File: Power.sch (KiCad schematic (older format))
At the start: 18 parts, among them P1 24 Pin MiniFit JR, SW1 Power Switch

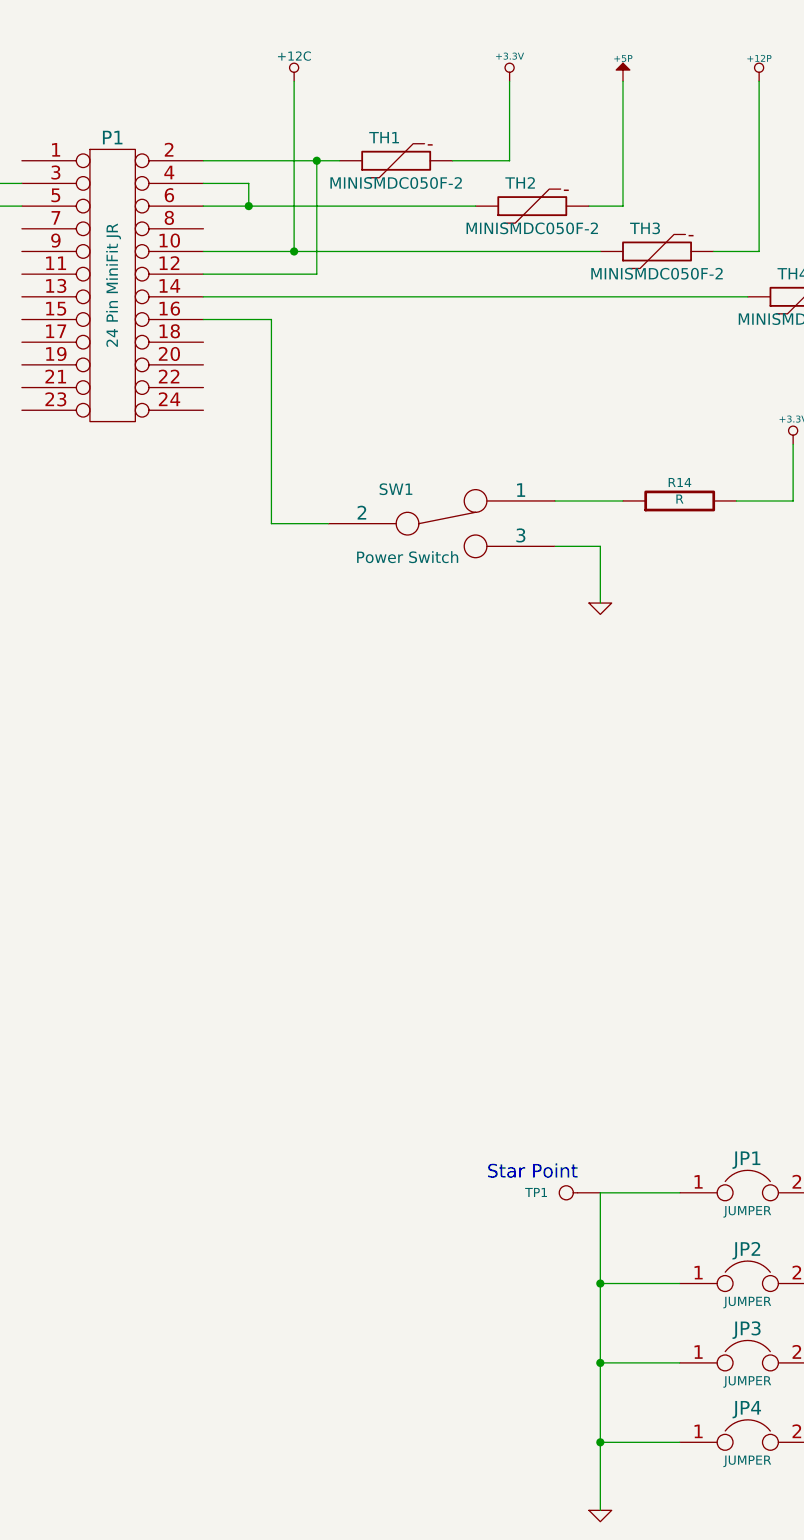
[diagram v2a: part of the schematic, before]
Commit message: Layout Work Session 16
Added ground connect to heatsink, fixed relay trace width, fixed silk
screen issues.
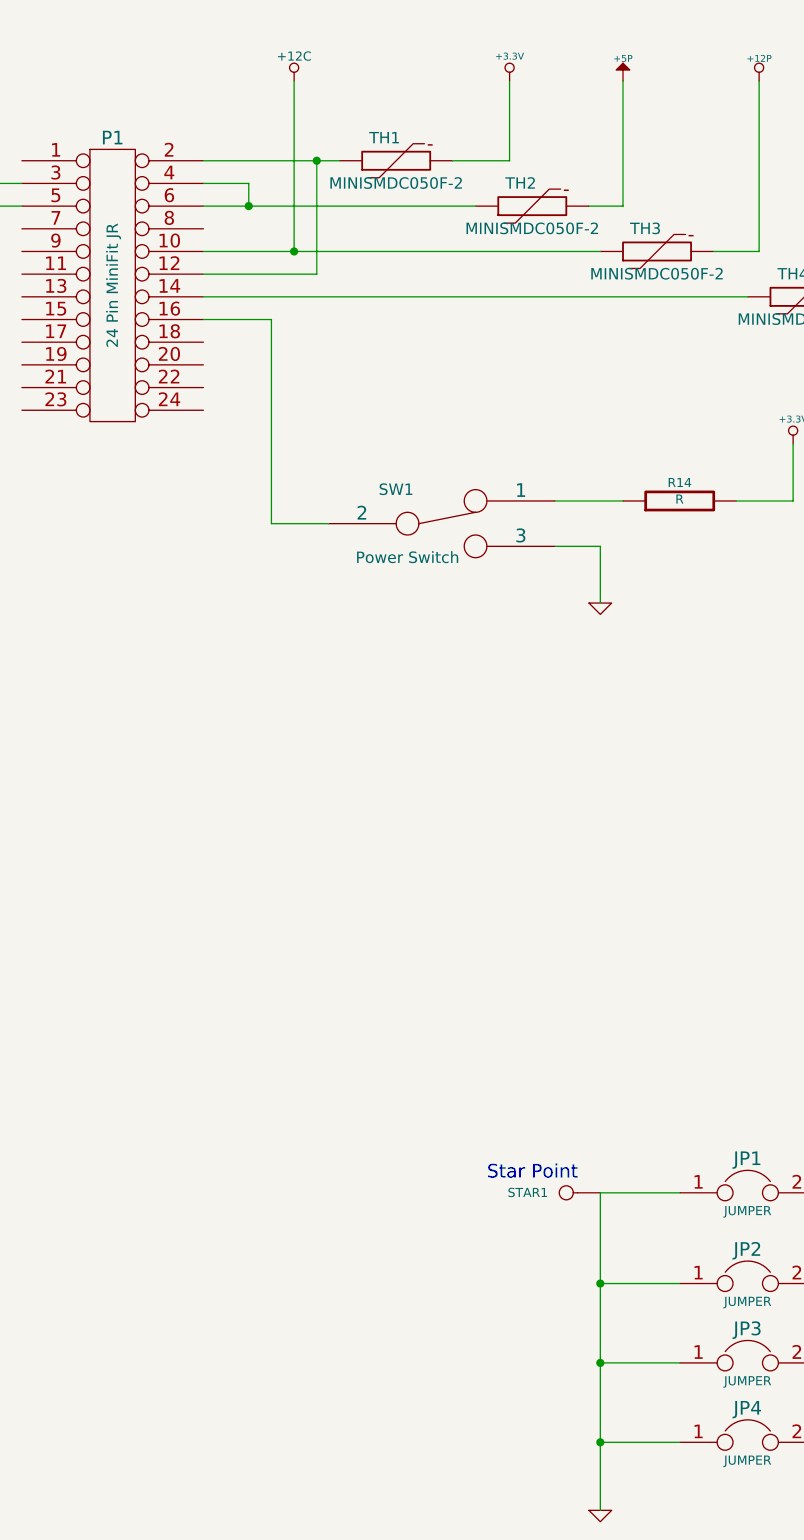
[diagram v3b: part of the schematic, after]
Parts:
- renumbered TP1 to STAR1
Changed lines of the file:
@@
-EESchema Schematic File Version 2  date 11/24/2013 8:21:44 PM
+EESchema Schematic File Version 2  date 12/1/2013 9:10:28 PM
 LIBS:power
 LIBS:device
@@
 Sheet 9 9
 Title ""
-Date "24 nov 2013"
+Date "2 dec 2013"
 Rev ""
 Comp ""
@@
 $EndComp
 $Comp
-L GND #PWR045
+L GND #PWR53
 U 1 1 523DFA76
 P 1400 1850
-F 0 "#PWR045" H 1400 1850 30  0001 C CNN
+F 0 "#PWR53" H 1400 1850 30  0001 C CNN
 F 1 "GND" H 1400 1780 30  0001 C CNN
 F 2 "" H 1400 1850 60  0000 C CNN
@@
 	1400 1600 1400 1850
 Wire Wire Line
-	3650 1500 3050 1500
+	3050 1500 3650 1500
 Wire Wire Line
 	4150 1500 4400 1500
@@
 	5500 1900 5500 1150
 $Comp
-L +12P #PWR046
+L +12P #PWR59
 U 1 1 523DFB91
 P 5500 1150
-F 0 "#PWR046" H 5500 1120 30  0001 C CNN
+F 0 "#PWR59" H 5500 1120 30  0001 C CNN
 F 1 "+12P" H 5500 1250 30  0000 C CNN
 F 2 "" H 5500 1150 60  0000 C CNN
@@
 $EndComp
 $Comp
-L -12P #PWR047
+L -12P #PWR61
 U 1 1 523E04D8
 P 6100 1150
-F 0 "#PWR047" H 6100 1280 20  0001 C CNN
+F 0 "#PWR61" H 6100 1280 20  0001 C CNN
 F 1 "-12P" H 6100 1250 30  0000 C CNN
 F 2 "" H 6100 1150 60  0000 C CNN
@@
 	4800 3200 4800 3450
 $Comp
-L GND #PWR048
+L GND #PWR56
 U 1 1 523E08C4
 P 4800 3450
-F 0 "#PWR048" H 4800 3450 30  0001 C CNN
+F 0 "#PWR56" H 4800 3450 30  0001 C CNN
 F 1 "GND" H 4800 3380 30  0001 C CNN
 F 2 "" H 4800 3450 60  0000 C CNN
@@
 	5650 3000 5650 2750
 $Comp
-L +3.3V #PWR049
+L +3.3V #PWR60
 U 1 1 523E0910
 P 5650 2750
-F 0 "#PWR049" H 5650 2710 30  0001 C CNN
+F 0 "#PWR60" H 5650 2710 30  0001 C CNN
 F 1 "+3.3V" H 5650 2860 30  0000 C CNN
 F 2 "" H 5650 2750 60  0000 C CNN
@@
 $EndComp
 $Comp
-L +12P #PWR050
+L +12P #PWR67
 U 1 1 523E0C76
 P 8000 2250
-F 0 "#PWR050" H 8000 2220 30  0001 C CNN
+F 0 "#PWR67" H 8000 2220 30  0001 C CNN
 F 1 "+12P" H 8000 2350 30  0000 C CNN
 F 2 "" H 8000 2250 60  0000 C CNN
@@
 $EndComp
 $Comp
-L -12P #PWR051
+L -12P #PWR68
 U 1 1 523E0C7C
 P 8000 3800
-F 0 "#PWR051" H 8000 3930 20  0001 C CNN
+F 0 "#PWR68" H 8000 3930 20  0001 C CNN
 F 1 "-12P" H 8000 3900 30  0000 C CNN
 F 2 "" H 8000 3800 60  0000 C CNN
@@
 $EndComp
 $Comp
-L GND #PWR052
+L GND #PWR69
 U 1 1 523E0C82
 P 9000 3200
-F 0 "#PWR052" H 9000 3200 30  0001 C CNN
+F 0 "#PWR69" H 9000 3200 30  0001 C CNN
 F 1 "GND" H 9000 3130 30  0001 C CNN
 F 2 "" H 9000 3200 60  0000 C CNN
@@
 Connection ~ 9450 3050
 $Comp
-L -12V #PWR053
+L -12V #PWR73
 U 1 1 523E0DD3
 P 10350 3800
-F 0 "#PWR053" H 10350 3930 20  0001 C CNN
+F 0 "#PWR73" H 10350 3930 20  0001 C CNN
 F 1 "-12V" H 10350 3900 30  0000 C CNN
 F 2 "" H 10350 3800 60  0000 C CNN
@@
 Connection ~ 9450 2450
 $Comp
-L +12V #PWR054
+L +12V #PWR72
 U 1 1 523E0E37
 P 10350 2200
-F 0 "#PWR054" H 10350 2150 20  0001 C CNN
+F 0 "#PWR72" H 10350 2150 20  0001 C CNN
 F 1 "+12V" H 10350 2300 30  0000 C CNN
 F 2 "" H 10350 2200 60  0000 C CNN
@@
 Connection ~ 3450 1900
 $Comp
-L +12C #PWR055
+L +12C #PWR54
 U 1 1 52438F0D
 P 3450 1150
-F 0 "#PWR055" H 3450 1120 30  0001 C CNN
+F 0 "#PWR54" H 3450 1120 30  0001 C CNN
 F 1 "+12C" H 3450 1260 40  0000 C CNN
 F 2 "~" H 3450 1150 60  0000 C CNN
@@
 $EndComp
 $Comp
-L GND #PWR056
+L GND #PWR70
 U 1 1 524502FC
 P 9400 1650
-F 0 "#PWR056" H 9400 1650 30  0001 C CNN
+F 0 "#PWR70" H 9400 1650 30  0001 C CNN
 F 1 "GND" H 9400 1580 30  0001 C CNN
 F 2 "" H 9400 1650 60  0000 C CNN
@@
 Connection ~ 9400 900
 $Comp
-L +5P #PWR56
+L +5P #PWR58
 U 1 1 52450355
 P 4900 1150
-F 0 "#PWR56" H 4900 1280 20  0001 C CNN
+F 0 "#PWR58" H 4900 1280 20  0001 C CNN
 F 1 "+5P" H 4900 1250 30  0000 C CNN
 F 2 "~" H 4900 1150 60  0000 C CNN
@@
 $EndComp
 $Comp
-L +5P #PWR64
+L +5P #PWR66
 U 1 1 52450371
 P 7950 700
-F 0 "#PWR64" H 7950 830 20  0001 C CNN
+F 0 "#PWR66" H 7950 830 20  0001 C CNN
 F 1 "+5P" H 7950 800 30  0000 C CNN
 F 2 "~" H 7950 700 60  0000 C CNN
@@
 $EndComp
 $Comp
-L +5V #PWR057
+L +5V #PWR71
 U 1 1 524503B6
 P 10300 650
-F 0 "#PWR057" H 10300 740 20  0001 C CNN
+F 0 "#PWR71" H 10300 740 20  0001 C CNN
 F 1 "+5V" H 10300 740 30  0000 C CNN
 F 2 "~" H 10300 650 60  0000 C CNN
@@
 $EndComp
 $Comp
-L +3.3V #PWR058
+L +3.3V #PWR55
 U 1 1 526E168C
 P 4400 1150
-F 0 "#PWR058" H 4400 1110 30  0001 C CNN
+F 0 "#PWR55" H 4400 1110 30  0001 C CNN
 F 1 "+3.3V" H 4400 1260 30  0000 C CNN
 F 2 "" H 4400 1150 60  0000 C CNN
@@
 Connection ~ 3550 1500
 $Comp
-L CONN_1 TP1
+L CONN_1 STAR1
 U 1 1 527EFE16
 P 4650 6050
-F 0 "TP1" H 4730 6050 40  0000 L CNN
+F 0 "STAR1" H 4730 6050 40  0000 L CNN
 F 1 "CONN_1" H 4650 6105 30  0001 C CNN
 F 2 "" H 4650 6050 60  0000 C CNN
@@
 $EndComp
 $Comp
-L GND #PWR059
+L GND #PWR57
 U 1 1 52804AA7
 P 4800 7450
-F 0 "#PWR059" H 4800 7450 30  0001 C CNN
+F 0 "#PWR57" H 4800 7450 30  0001 C CNN
 F 1 "GND" H 4800 7380 30  0001 C CNN
 F 2 "" H 4800 7450 60  0000 C CNN
@@
 $EndComp
 Wire Wire Line
-	4800 7450 4800 6050
+	4800 6050 4800 7450
 Wire Wire Line
 	4800 6050 5150 6050
@@
 	5750 6050 6200 6050
 $Comp
-L GND_RELAY #PWR060
+L GND_RELAY #PWR65
 U 1 1 52804C2C
 P 6200 7400
-F 0 "#PWR060" H 6200 7400 30  0001 C CNN
+F 0 "#PWR65" H 6200 7400 30  0001 C CNN
 F 1 "GND_RELAY" H 6200 7330 30  0000 C CNN
 F 2 "~" H 6200 7400 60  0000 C CNN
@@
 $EndComp
 $Comp
-L GND_LED #PWR061
+L GND_LED #PWR64
 U 1 1 52804C3B
 P 6200 6950
-F 0 "#PWR061" H 6200 6950 30  0001 C CNN
+F 0 "#PWR64" H 6200 6950 30  0001 C CNN
 F 1 "GND_LED" H 6200 6880 30  0000 C CNN
 F 2 "~" H 6200 6950 60  0000 C CNN
@@
 $EndComp
 $Comp
-L GND_PWR #PWR062
+L GND_PWR #PWR63
 U 1 1 52804C4A
 P 6200 6550
-F 0 "#PWR062" H 6200 6550 30  0001 C CNN
+F 0 "#PWR63" H 6200 6550 30  0001 C CNN
 F 1 "GND_PWR" H 6200 6480 30  0000 C CNN
 F 2 "~" H 6200 6550 60  0000 C CNN
@@
 $EndComp
 $Comp
-L AGND #PWR063
+L AGND #PWR62
 U 1 1 52804C59
 P 6200 6200
-F 0 "#PWR063" H 6200 6200 40  0001 C CNN
+F 0 "#PWR62" H 6200 6200 40  0001 C CNN
 F 1 "AGND" H 6200 6130 50  0000 C CNN
 F 2 "~" H 6200 6200 60  0000 C CNN

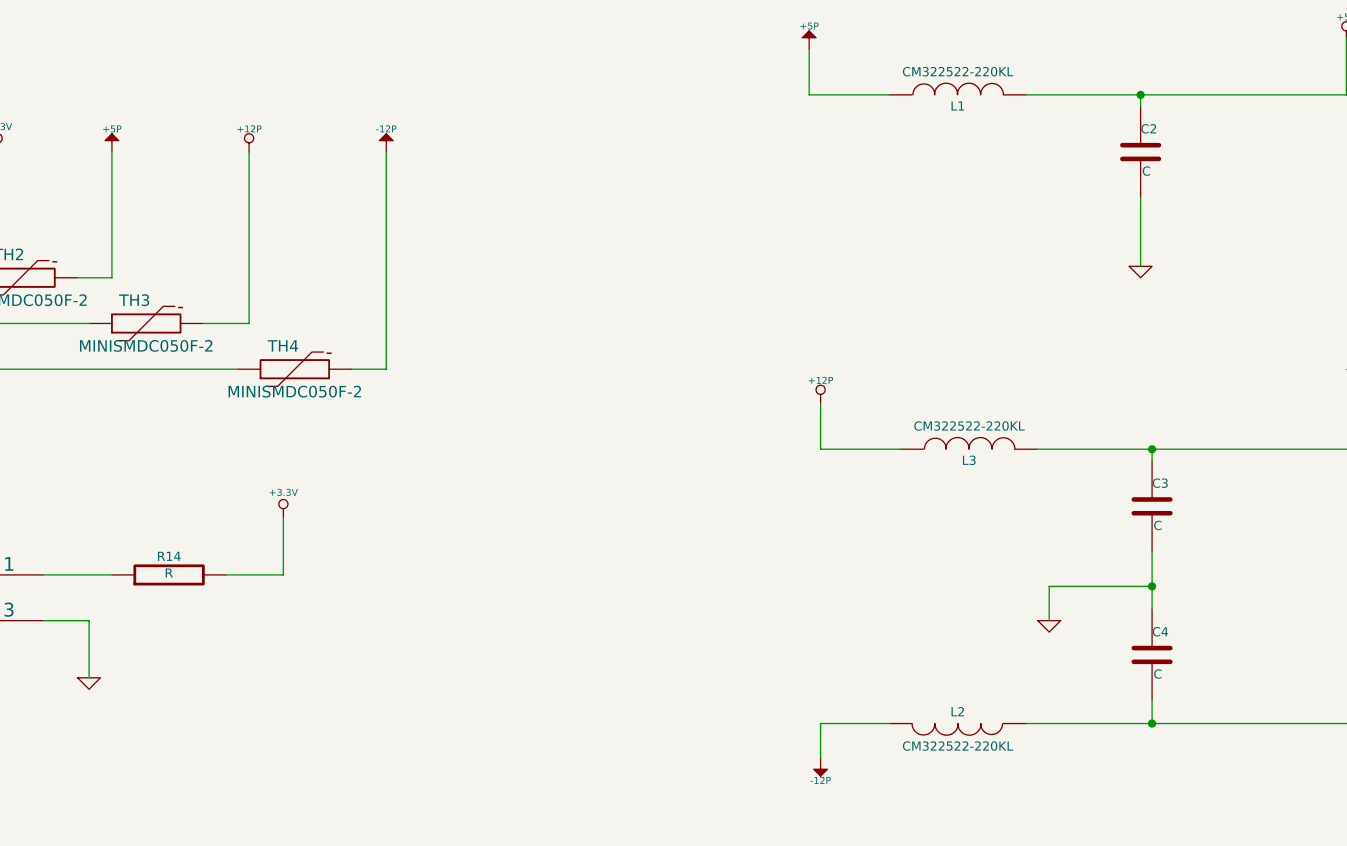
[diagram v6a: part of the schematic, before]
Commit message: Added Passive Values and SPICE models
As part of week 1 of Session 1B, we added a SPICE model of the In amp
and went through and assigned values to all of the passive components.
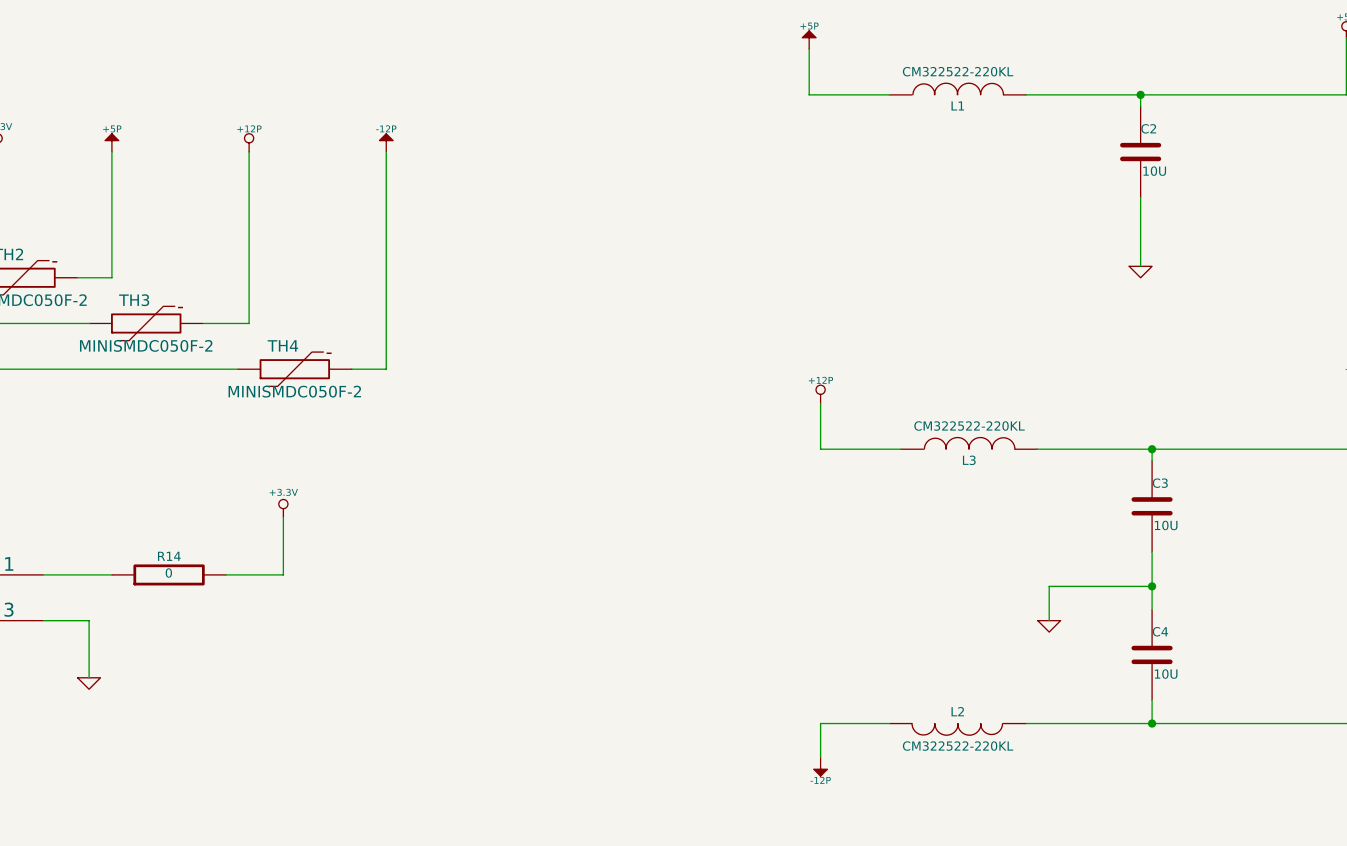
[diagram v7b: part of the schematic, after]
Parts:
- C2, C3, C4: value C -> 10U
- R14: value R -> 0
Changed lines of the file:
@@
-EESchema Schematic File Version 2  date 2/16/2014 3:41:32 PM
+EESchema Schematic File Version 2  date 4/16/2014 11:04:06 PM
 LIBS:power
 LIBS:device
@@
 Sheet 9 9
 Title ""
-Date "16 feb 2014"
+Date "17 apr 2014"
 Rev ""
 Comp ""
@@
 P 5150 3000
 F 0 "R14" V 5230 3000 40  0000 C CNN
-F 1 "R" V 5157 3001 40  0000 C CNN
+F 1 "0" V 5157 3001 40  0000 C CNN
 F 2 "~" V 5080 3000 30  0000 C CNN
 F 3 "~" H 5150 3000 30  0000 C CNN
@@
 P 9450 2700
 F 0 "C3" H 9450 2800 40  0000 L CNN
-F 1 "C" H 9456 2615 40  0000 L CNN
+F 1 "10U" H 9456 2615 40  0000 L CNN
 F 2 "~" H 9488 2550 30  0000 C CNN
 F 3 "~" H 9450 2700 60  0000 C CNN
@@
 P 9450 3350
 F 0 "C4" H 9450 3450 40  0000 L CNN
-F 1 "C" H 9456 3265 40  0000 L CNN
+F 1 "10U" H 9456 3265 40  0000 L CNN
 F 2 "~" H 9488 3200 30  0000 C CNN
 F 3 "~" H 9450 3350 60  0000 C CNN
@@
 P 9400 1150
 F 0 "C2" H 9400 1250 40  0000 L CNN
-F 1 "C" H 9406 1065 40  0000 L CNN
+F 1 "10U" H 9406 1065 40  0000 L CNN
 F 2 "~" H 9438 1000 30  0000 C CNN
 F 3 "~" H 9400 1150 60  0000 C CNN
